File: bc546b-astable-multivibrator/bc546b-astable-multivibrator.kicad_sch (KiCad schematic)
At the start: 13 parts

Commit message: Reviewed schematics and boards
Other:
- note added: "Co się stanie, gdy tranzystor będzie zamknięty, a dioda będzie świecić (I2 low) ? :)"
- note added: "PS. kondensator wybuchnie Ci w twarz"
- note added: "Zweryfikuj sobie połączenia"
- note added: "https://www.fuw.edu.pl/wo/data/prac-fiz-multiwibr-asta.pdf"
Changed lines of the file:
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@@
     (fill (type none))
+  )
+  (text "Co się stanie, gdy tranzystor będzie zamknięty, a dioda będzie świecić (I2 low) ? :)"
+    (at 91.44 63.5 0)
+    (effects (font (size 1.27 1.27) (color 255 7 53 1)) (justify left bottom))
+  )
+  (text "https://www.fuw.edu.pl/wo/data/prac-fiz-multiwibr-asta.pdf"
+    (at 96.52 86.36 0)
+    (effects (font (size 1.27 1.27) (color 255 3 22 1)) (justify left bottom))
+  )
+  (text "Zweryfikuj sobie połączenia" (at 96.52 88.9 0)
+    (effects (font (size 1.27 1.27) (color 255 0 2 1)) (justify left bottom))
+  )
+  (text "PS. kondensator wybuchnie Ci w twarz" (at 91.44 66.04 0)
+    (effects (font (size 1.27 1.27) (color 255 8 35 1)) (justify left bottom))
   )
   (text "Battery" (at 16.51 20.32 0)

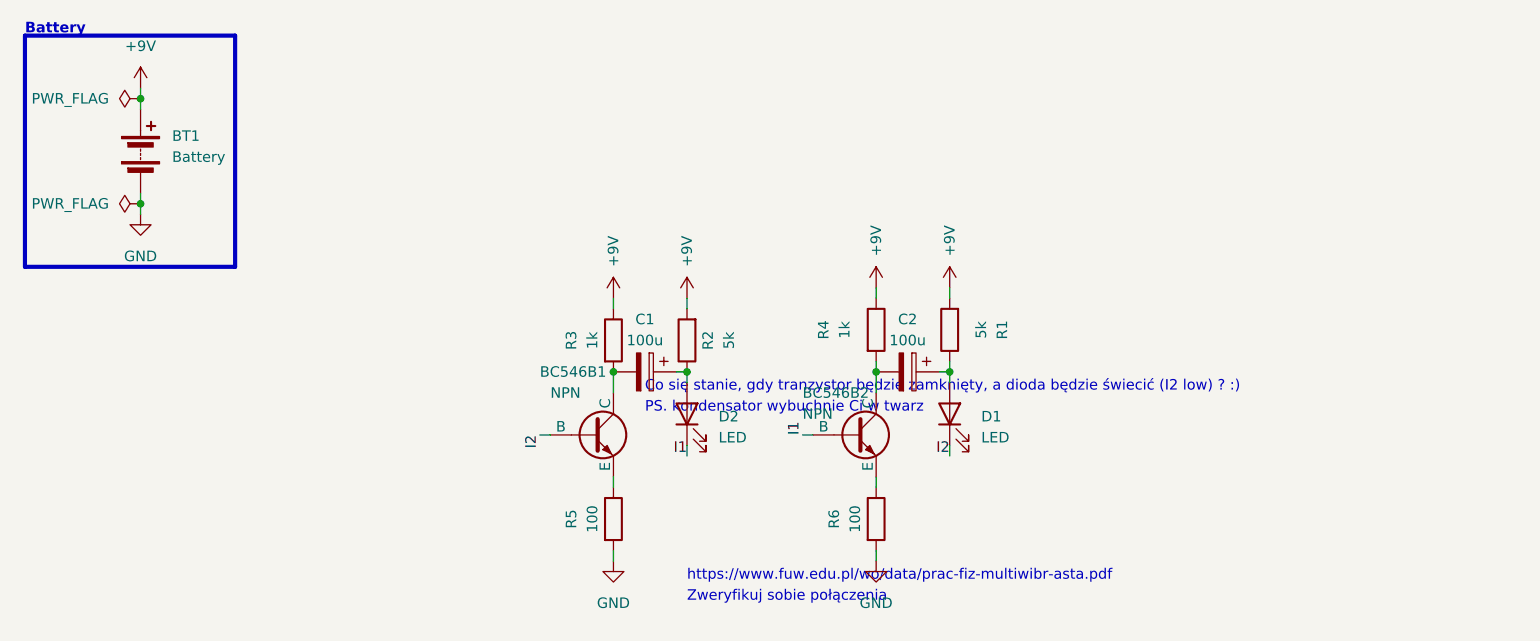
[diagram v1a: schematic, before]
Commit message: project 6 / bc546b astable multivibrator / improved schematics, pcb after review
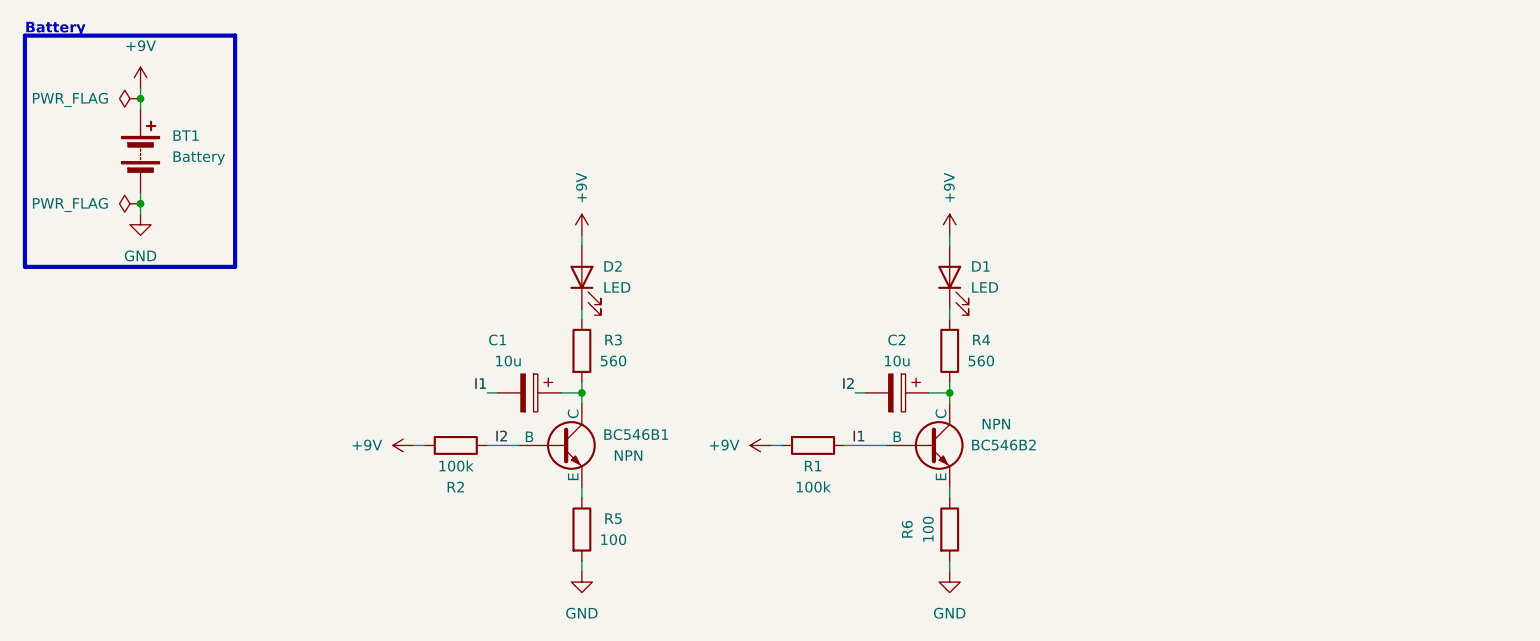
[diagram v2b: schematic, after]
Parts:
- C1, C2: value 100u -> 10u
- R1, R2: value 5k -> 100k
- R3, R4: value 1k -> 560
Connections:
- net +9V: now also D1.2 (A), D2.2 (A); no longer R3.1, R4.1
- net I1: now also C1.2, R1.1; no longer D2.1 (K)
- net I2: now also C2.2, R2.1; no longer D1.1 (K)
- net at BC546B1.1 (C), R3.2: now also C1.1; no longer C1.2
- new net: D2.1 (K), R3.1
- new net: BC546B2.1 (C), C2.1, R4.1
- new net: D1.1 (K), R4.2
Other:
- note removed: "Co się stanie, gdy tranzystor będzie zamknięty, a dioda będzie świecić (I2 low) ? :)"
- note removed: "PS. kondensator wybuchnie Ci w twarz"
- note removed: "Zweryfikuj sobie połączenia"
- note removed: "https://www.fuw.edu.pl/wo/data/prac-fiz-multiwibr-asta.pdf"
- moved on the sheet: BC546B1, BC546B2, R1, R3, R5, R6
